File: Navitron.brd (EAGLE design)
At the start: 70 x 70 mm, 92 parts, among them J2 DX07S016JA1R1500, Q1 ROHM_RUM002N02T2LROHM_RUM002N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, Q2 2.5A/30V, Q3 ROHM_RUM002N02T2LROHM_RUM002N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, Q4 ROHM_RUM002N02T2LROHM_RUM002N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, Q5 ROHM_RUM002N02T2LROHM_RUM002N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, T1 BC847, T2 BC847, U3 MCP73831, U5 CH340C

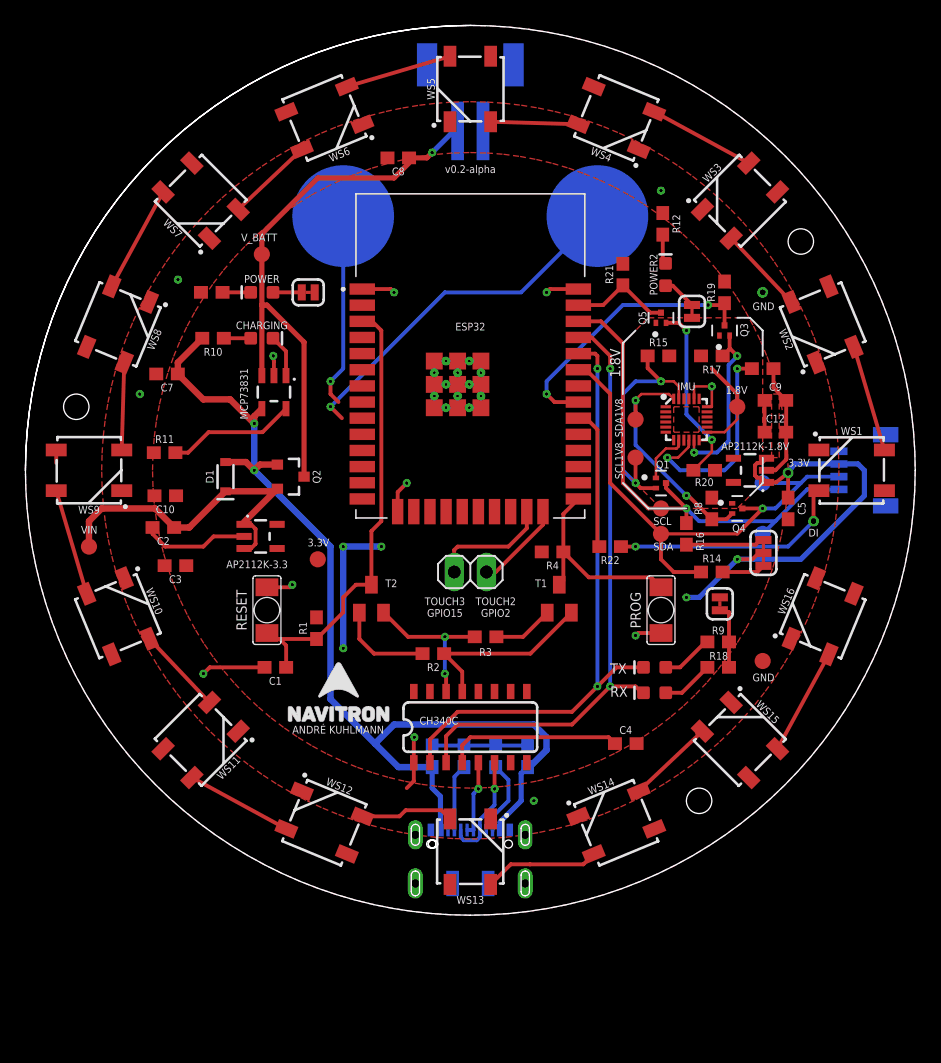
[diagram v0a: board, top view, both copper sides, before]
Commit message: Connect Touch Pad 8 & 9 and DRC Check
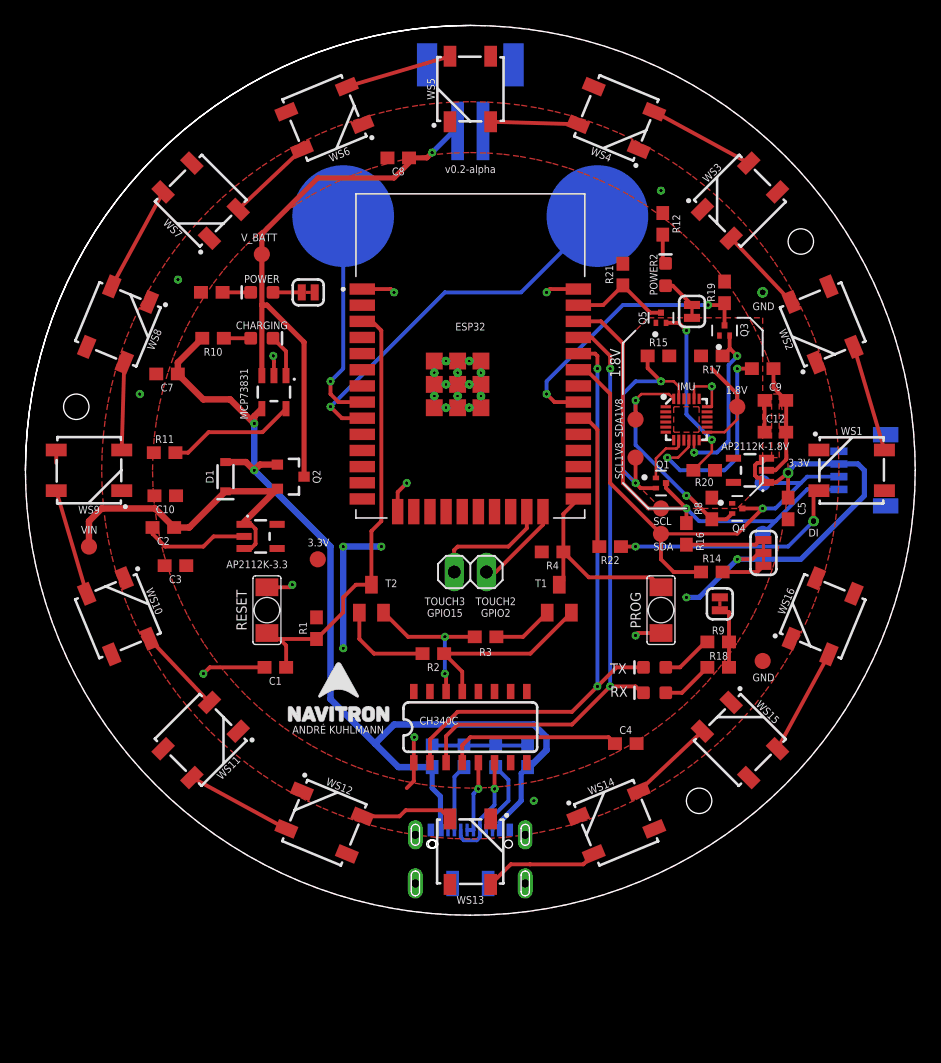
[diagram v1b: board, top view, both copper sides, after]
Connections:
- removed net TOUCH8: TOUCH1.TOUCH
- removed net TOUCH9: TOUCH2.TOUCH
- net T8: now also TOUCH1.TOUCH
- net T9: now also TOUCH2.TOUCH
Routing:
- net T9: track 0.00 -> 30.1 mm, vias 0 -> 1
- net TOUCH9: track 28.5 -> 0.00 mm, vias 1 -> 0
- net T8: track 0.00 -> 17.2 mm, vias 0 -> 1
- net TOUCH8: track 15.3 -> 0.00 mm, vias 1 -> 0
- net WS14_15: track 7.41 -> 6.89 mm
- net WS8_9: track 7.41 -> 6.89 mm
- net WS10_11: track 7.41 -> 6.89 mm
- net SCL: track 40.2 -> 39.7 mm
- net 3.3V: track 46.8 -> 46.3 mm
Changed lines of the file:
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@@
 <layer number="20" name="Dimension" color="24" fill="1" visible="yes" active="yes"/>
 <layer number="21" name="tPlace" color="7" fill="1" visible="yes" active="yes"/>
-<layer number="22" name="bPlace" color="7" fill="1" visible="yes" active="yes"/>
+<layer number="22" name="bPlace" color="7" fill="1" visible="no" active="yes"/>
 <layer number="23" name="tOrigins" color="15" fill="1" visible="yes" active="yes"/>
 <layer number="24" name="bOrigins" color="15" fill="1" visible="no" active="yes"/>
@@
 <contactref element="R1" pad="1"/>
 <contactref element="T2" pad="3"/>
-<wire x1="27.22" y1="26" x2="27.17" y2="26.05" width="0.3048" layer="1"/>
 <wire x1="27.22" y1="26" x2="27.22" y2="30.22" width="0.3048" layer="1"/>
 <wire x1="27.22" y1="30.22" x2="28" y2="31" width="0.3048" layer="1"/>
@@
 <vertex x="60" y="35" curve="-90"/>
 </polygon>
-<wire x1="64.5" y1="35.5" x2="64" y2="35.5" width="0.3048" layer="16"/>
 <contactref element="C10" pad="1"/>
 <contactref element="R21" pad="2"/>
@@
 <wire x1="66" y1="33" x2="66" y2="35" width="0.4064" layer="16"/>
 <wire x1="66" y1="35" x2="65.5" y2="35.5" width="0.4064" layer="16"/>
-<wire x1="65.5" y1="35.5" x2="64" y2="35.5" width="0.4064" layer="16"/>
 <wire x1="56" y1="28" x2="61" y2="28" width="0.4064" layer="16"/>
 <contactref element="AP2112K-1.8V" pad="1"/>
@@
 <vertex x="59.3" y="36"/>
 </polygon>
+<wire x1="65.5" y1="35.5" x2="64" y2="35.5" width="0.4064" layer="16"/>
 </signal>
 <signal name="TO_T2">
@@
 <contactref element="ESP32" pad="36"/>
 <contactref element="J3" pad="4"/>
-<wire x1="64" y1="33.5" x2="63.5" y2="33.5" width="0.2032" layer="16"/>
 <contactref element="Q1" pad="3"/>
 <contactref element="R16" pad="1"/>
-<wire x1="64" y1="33.5" x2="61.5" y2="33.5" width="0.3048" layer="16"/>
 <via x="52" y="32" extent="1-16" drill="0.25"/>
 <wire x1="50.4" y1="33.6" x2="52" y2="32" width="0.3048" layer="1"/>
@@
 <wire x1="59" y1="31" x2="53" y2="31" width="0.3048" layer="16"/>
 <wire x1="53" y1="31" x2="52" y2="32" width="0.3048" layer="16"/>
-<wire x1="61.5" y1="33.5" x2="59" y2="31" width="0.3048" layer="16"/>
+<wire x1="59" y1="31" x2="61.5" y2="33.5" width="0.3048" layer="16"/>
 <wire x1="49" y1="32" x2="47" y2="34" width="0.3048" layer="1"/>
 <wire x1="47" y1="34" x2="47" y2="45" width="0.3048" layer="1"/>
@@
 <contactref element="SCL1" pad="TP"/>
 <wire x1="58" y1="30" x2="59" y2="31" width="0.3048" layer="16"/>
+<wire x1="61.5" y1="33.5" x2="64" y2="33.5" width="0.3048" layer="16"/>
 </signal>
 <signal name="VIN">
@@
 <wire x1="18" y1="38.683" x2="16.103" y2="40.58" width="0.508" layer="1"/>
 <wire x1="16.103" y1="40.58" x2="13.99" y2="40.58" width="0.508" layer="1"/>
-<wire x1="13.91" y1="45.39" x2="14" y2="45.3" width="0.3048" layer="1"/>
 <wire x1="15.74" y1="35.65" x2="17.35" y2="35.65" width="0.508" layer="1"/>
 <wire x1="17.35" y1="35.65" x2="18" y2="35" width="0.508" layer="1"/>
@@
 <wire x1="31.58" y1="59.58" x2="30.18" y2="59.58" width="0.4064" layer="1"/>
 <wire x1="18.6" y1="42.4501" x2="18.6" y2="48" width="0.4064" layer="1"/>
-<wire x1="18.6" y1="48" x2="18.6" y2="53.6" width="0.4064" layer="1"/>
+<wire x1="18.6" y1="48" x2="18.6" y2="52" width="0.4064" layer="1"/>
+<wire x1="18.6" y1="52" x2="18.6" y2="53.6" width="0.4064" layer="1"/>
 <wire x1="23" y1="58" x2="29" y2="58" width="0.4064" layer="1"/>
 <wire x1="29" y1="58" x2="30.18" y2="59.18" width="0.4064" layer="1"/>
@@
 <wire x1="19" y1="48" x2="18.6" y2="48" width="0.4064" layer="1"/>
 <contactref element="V_BATT" pad="TP"/>
-<wire x1="18.6" y1="42.4501" x2="18.6" y2="52" width="0" layer="19" extent="1-1"/>
 </signal>
 <signal name="CHAR_LED_VIN">
@@
 <polygon width="0.15" layer="1">
 <vertex x="49" y="47"/>
-<vertex x="57" y="47"/>
-<vertex x="58" y="46"/>
+<vertex x="58" y="47"/>
 <vertex x="58" y="34"/>
 <vertex x="56" y="32"/>
@@
 <contactref element="R20" pad="2"/>
 <wire x1="58.15" y1="40.5" x2="58.15" y2="38" width="0.3048" layer="1"/>
-<wire x1="52.44" y1="46.992" x2="52.448" y2="47" width="0.3048" layer="1"/>
 <contactref element="AP2112K-1.8V" pad="5"/>
 <contactref element="1.8V" pad="TP"/>
@@
 <contactref element="WS8" pad="2"/>
 <contactref element="WS9" pad="4"/>
-<wire x1="7.577" y1="43.007803125" x2="7.77564375" y2="43.487371875" width="0.2" layer="1" curve="-45"/>
 <wire x1="7.577" y1="36.6" x2="7.77564375" y2="43.487371875" width="0.3048" layer="1"/>
 </signal>
@@
 <contactref element="WS10" pad="2"/>
 <contactref element="WS11" pad="4"/>
-<wire x1="9.9466375" y1="21.27138125" x2="9.74799375" y2="21.75095" width="0.2" layer="1" curve="-45"/>
 <wire x1="14.4776375" y1="16.74038125" x2="9.74799375" y2="21.75095" width="0.3048" layer="1"/>
 </signal>
@@
 <contactref element="WS14" pad="2"/>
 <contactref element="WS15" pad="4"/>
-<wire x1="52.780046875" y1="14.27899375" x2="53.259615625" y2="14.4776375" width="0.2" layer="1" curve="-45"/>
 <wire x1="48.249046875" y1="9.74799375" x2="53.259615625" y2="14.4776375" width="0.3048" layer="1"/>
 </signal>
@@
 <contactref element="IMU" pad="7"/>
 </signal>
-<signal name="TOUCH8">
-<contactref element="TOUCH1" pad="TOUCH"/>
-<wire x1="25" y1="55" x2="25" y2="43" width="0.3048" layer="16"/>
-<wire x1="25" y1="43" x2="24" y2="42" width="0.3048" layer="16"/>
-<via x="24" y="42" extent="1-16" drill="0.25"/>
-<wire x1="24" y1="42" x2="24" y2="41" width="0.3048" layer="1"/>
-<wire x1="24" y1="41" x2="24.63" y2="40.37" width="0.3048" layer="1"/>
-</signal>
-<signal name="TOUCH9">
-<contactref element="TOUCH2" pad="TOUCH"/>
-<wire x1="45" y1="55" x2="39" y2="49" width="0.3048" layer="16"/>
-<wire x1="33" y1="49" x2="24" y2="40" width="0.3048" layer="16"/>
-<via x="24" y="40" extent="1-16" drill="0.25"/>
-<wire x1="24" y1="40" x2="24.9" y2="39.1" width="0.3048" layer="1"/>
-<wire x1="39" y1="49" x2="33" y2="49" width="0.3048" layer="16"/>
-</signal>
 <signal name="T2">
 <contactref element="ESP32" pad="24"/>
@@
 <signal name="T8">
 <contactref element="ESP32" pad="8"/>
+<contactref element="TOUCH1" pad="TOUCH"/>
+<wire x1="25" y1="55" x2="25" y2="43" width="0.3048" layer="16"/>
+<wire x1="25" y1="43" x2="24" y2="42" width="0.3048" layer="16"/>
+<via x="24" y="42" extent="1-16" drill="0.25"/>
+<wire x1="24" y1="42" x2="24" y2="41" width="0.3048" layer="1"/>
+<wire x1="24" y1="41" x2="24.63" y2="40.37" width="0.3048" layer="1"/>
+<wire x1="24.63" y1="40.37" x2="26.5" y2="40.37" width="0.3048" layer="1"/>
 </signal>
 <signal name="T9">
 <contactref element="ESP32" pad="9"/>
+<contactref element="TOUCH2" pad="TOUCH"/>
+<wire x1="45" y1="55" x2="39" y2="49" width="0.3048" layer="16"/>
+<wire x1="33" y1="49" x2="24" y2="40" width="0.3048" layer="16"/>
+<via x="24" y="40" extent="1-16" drill="0.25"/>
+<wire x1="24" y1="40" x2="24.9" y2="39.1" width="0.3048" layer="1"/>
+<wire x1="39" y1="49" x2="33" y2="49" width="0.3048" layer="16"/>
+<wire x1="24.9" y1="39.1" x2="26.5" y2="39.1" width="0.3048" layer="1"/>
 </signal>
 </signals>
